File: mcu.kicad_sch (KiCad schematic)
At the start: 46 parts, among them J1 10118193-0001LF, J5 Conn_ARM_SWD_TagConnect_TC2030, SW1 SW_Push, SW2 SW_Push, SW3 SW_Push, U1 RP2040, U2 AP2112K-3.3TRG1, U3 W25Q16JVSSIQ, Y3 12MHZ

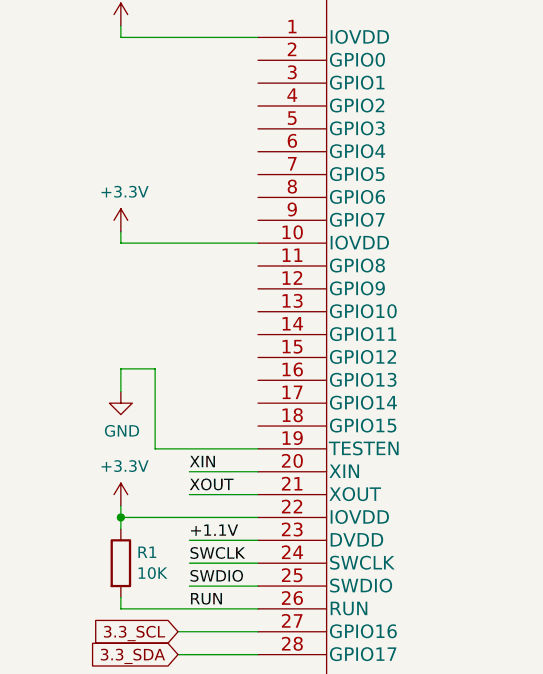
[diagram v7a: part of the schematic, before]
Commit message: Add mcp 2517 can transceiver
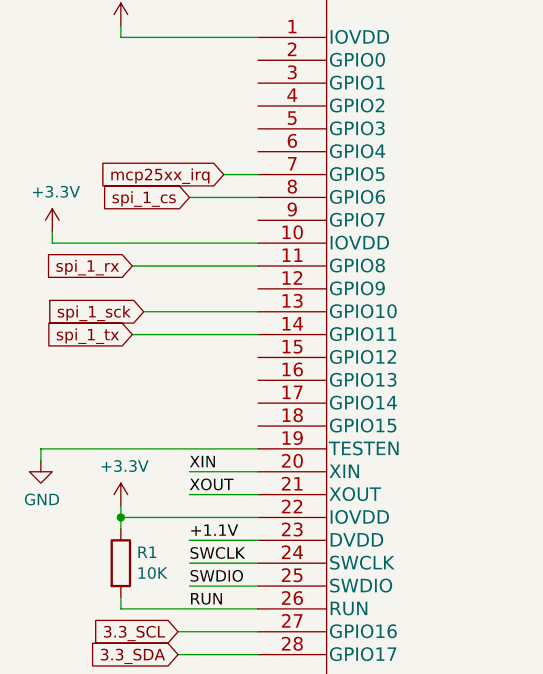
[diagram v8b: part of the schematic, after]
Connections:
- net spi_1_rx: now reaches U1.11 (GPIO8)
- net spi_1_sck: now reaches U1.13 (GPIO10)
- net spi_1_tx: now reaches U1.14 (GPIO11)
- net mcp25xx_irq: now reaches U1.7 (GPIO5)
- net spi_1_cs: now reaches U1.8 (GPIO6)
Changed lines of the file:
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@@
+    (stroke (width 0) (type default))
+  )
+  (wire (pts (xy 35.56 127) (xy 39.37 127))
     (stroke (width 0) (type default))
   )
@@
     (stroke (width 0) (type default))
   )
-  (wire (pts (xy 27.94 148.59) (xy 24.13 148.59))
+  (wire (pts (xy 15.24 157.48) (xy 39.37 157.48))
     (stroke (width 0) (type default))
   )
@@
     (stroke (width 0) (type default))
   )
+  (wire (pts (xy 31.75 129.54) (xy 39.37 129.54))
+    (stroke (width 0) (type default))
+  )
   (wire (pts (xy 207.01 138.43) (xy 196.85 138.43))
     (stroke (width 0) (type default))
@@
     (stroke (width 0) (type default))
   )
-  (wire (pts (xy 24.13 134.62) (xy 24.13 133.35))
+  (wire (pts (xy 16.51 134.62) (xy 16.51 133.35))
     (stroke (width 0) (type default))
   )
@@
     (stroke (width 0) (type default))
   )
-  (wire (pts (xy 39.37 157.48) (xy 27.94 157.48))
-    (stroke (width 0) (type default))
-  )
-  (wire (pts (xy 24.13 148.59) (xy 24.13 151.13))
+  (wire (pts (xy 15.24 157.48) (xy 15.24 158.75))
     (stroke (width 0) (type default))
   )
@@
     (stroke (width 0) (type default))
   )
+  (wire (pts (xy 25.4 137.16) (xy 39.37 137.16))
+    (stroke (width 0) (type default))
+  )
   (wire (pts (xy 232.41 87.63) (xy 220.98 87.63))
     (stroke (width 0) (type default))
@@
     (stroke (width 0) (type default))
   )
+  (wire (pts (xy 26.67 142.24) (xy 39.37 142.24))
+    (stroke (width 0) (type default))
+  )
   (wire (pts (xy 67.31 58.42) (xy 67.31 63.5))
     (stroke (width 0) (type default))
@@
     (stroke (width 0) (type default))
   )
-  (wire (pts (xy 24.13 134.62) (xy 39.37 134.62))
+  (wire (pts (xy 16.51 134.62) (xy 39.37 134.62))
     (stroke (width 0) (type default))
   )
@@
     (stroke (width 0) (type default))
   )
+  (wire (pts (xy 25.4 144.78) (xy 39.37 144.78))
+    (stroke (width 0) (type default))
+  )
   (wire (pts (xy 100.33 167.64) (xy 120.65 167.64))
     (stroke (width 0) (type default))
@@
   )
   (wire (pts (xy 186.69 87.63) (xy 175.26 87.63))
-    (stroke (width 0) (type default))
-  )
-  (wire (pts (xy 27.94 157.48) (xy 27.94 148.59))
     (stroke (width 0) (type default))
   )
@@
   (label "led_g" (at 208.28 62.23 180) (fields_autoplaced)
     (effects (font (size 1.27 1.27)) (justify right bottom))
+  )
+  (global_label "spi_1_rx" (shape input) (at 25.4 137.16 180)
+    (effects (font (size 1.27 1.27)) (justify right))
+    (property "Intersheetrefs" "${INTERSHEET_REFS}" (at 25.4 137.16 0)
+      (effects (font (size 1.27 1.27)) hide)
+    )
+  )
+  (global_label "mcp25xx_irq" (shape input) (at 35.56 127 180)
+    (effects (font (size 1.27 1.27)) (justify right))
+    (property "Intersheetrefs" "${INTERSHEET_REFS}" (at 35.56 127 0)
+      (effects (font (size 1.27 1.27)) hide)
+    )
+  )
+  (global_label "spi_1_tx" (shape input) (at 25.4 144.78 180)
+    (effects (font (size 1.27 1.27)) (justify right))
+    (property "Intersheetrefs" "${INTERSHEET_REFS}" (at 25.4 144.78 0)
+      (effects (font (size 1.27 1.27)) hide)
+    )
   )
   (global_label "3.3_SDA" (shape input) (at 30.48 180.34 180)
@@
     (effects (font (size 1.27 1.27)) (justify right))
     (property "Intersheetrefs" "${INTERSHEET_REFS}" (at 30.48 177.8 0)
+      (effects (font (size 1.27 1.27)) hide)
+    )
+  )
+  (global_label "spi_1_cs" (shape input) (at 31.75 129.54 180)
+    (effects (font (size 1.27 1.27)) (justify right))
+    (property "Intersheetrefs" "${INTERSHEET_REFS}" (at 31.75 129.54 0)
+      (effects (font (size 1.27 1.27)) hide)
+    )
+  )
+  (global_label "spi_1_sck" (shape input) (at 26.67 142.24 180)
+    (effects (font (size 1.27 1.27)) (justify right))
+    (property "Intersheetrefs" "${INTERSHEET_REFS}" (at 26.67 142.24 0)
       (effects (font (size 1.27 1.27)) hide)
     )
@@
     )
   )
-  (symbol (lib_id "power:GND") (at 24.13 151.13 0) (unit 1)
-    (in_bom yes) (on_board yes) (dnp no)
-    (property "Reference" "#PWR0107" (at 24.13 157.48 0)
-      (effects (font (size 1.27 1.27)) hide)
-    )
-    (property "Value" "GND" (at 24.257 155.5242 0)
-      (effects (font (size 1.27 1.27)))
-    )
-    (property "Footprint" "" (at 24.13 151.13 0)
-      (effects (font (size 1.27 1.27)) hide)
-    )
-    (property "Datasheet" "" (at 24.13 151.13 0)
+  (symbol (lib_id "power:GND") (at 15.24 158.75 0) (unit 1)
+    (in_bom yes) (on_board yes) (dnp no)
+    (property "Reference" "#PWR0107" (at 15.24 165.1 0)
+      (effects (font (size 1.27 1.27)) hide)
+    )
+    (property "Value" "GND" (at 15.367 163.1442 0)
+      (effects (font (size 1.27 1.27)))
+    )
+    (property "Footprint" "" (at 15.24 158.75 0)
+      (effects (font (size 1.27 1.27)) hide)
+    )
+    (property "Datasheet" "" (at 15.24 158.75 0)
       (effects (font (size 1.27 1.27)) hide)
     )
@@
     )
   )
-  (symbol (lib_id "rpi-pico-debugger-shoe-rescue:+3.3V-power") (at 24.13 133.35 0) (unit 1)
-    (in_bom yes) (on_board yes) (dnp no)
-    (property "Reference" "#PWR0109" (at 24.13 137.16 0)
-      (effects (font (size 1.27 1.27)) hide)
-    )
-    (property "Value" "+3.3V" (at 24.511 128.9558 0)
-      (effects (font (size 1.27 1.27)))
-    )
-    (property "Footprint" "" (at 24.13 133.35 0)
-      (effects (font (size 1.27 1.27)) hide)
-    )
-    (property "Datasheet" "" (at 24.13 133.35 0)
-      (effects (font (size 1.27 1.27)) hide)
-    )
+  (symbol (lib_id "rpi-pico-debugger-shoe-rescue:+3.3V-power") (at 16.51 133.35 0) (unit 1)
+    (in_bom yes) (on_board yes) (dnp no)
+    (property "Reference" "#PWR0109" (at 16.51 137.16 0)
+      (effects (font (size 1.27 1.27)) hide)
+    )
+    (property "Value" "+3.3V" (at 16.891 128.9558 0)
+      (effects (font (size 1.27 1.27)))
+    )
+    (property "Footprint" "" (at 16.51 133.35 0)
+      (effects (font (size 1.27 1.27)) hide)
+    )
+    (property "Datasheet" "" (at 16.51 133.35 0)
+      (effects (font (size 1.27 1.27)) hide)
+    )
